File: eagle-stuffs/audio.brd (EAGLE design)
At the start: 57.1 x 44.5 mm, 23 parts, among them IC2 TL084P, IC3 DS1804-50k, IC4 DS1804-100k, U2 SSM2211SZ

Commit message: Added some info
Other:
- board text added: "Rev. A"
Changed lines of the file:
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@@
 <hole x="54.61" y="2.54" drill="2.8"/>
 <rectangle x1="34.29" y1="26.67" x2="39.37" y2="29.21" layer="41"/>
+<text x="44.45" y="38.1" size="1.778" layer="25">Rev. A</text>
 </plain>
 <attributes>

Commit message: Final version
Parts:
- removed IN: (no value), pinhead:1X02
- removed U2: SSM2211SZ, Analog Devices_By_element14_Batch_1:SOIC127P600X175-8N
- added D1: 1N5817, adafruit:DO41-7
- added IC1: SSM2211SZ, Analog Devices_By_element14_Batch_1:SOIC127P600X175-8N
- added LINE-IN: (no value), pinhead:1X02
- added R1: 2k, rcl:0204V
- added R11: 100k, rcl:0204V
- added R12: 15k, rcl:0204V
- added R13: 5.1k, rcl:0204V
- added R14: 20k, rcl:0204V
- added R2: 1k, rcl:0204V
- C1: value 250u -> 250; device rcl:E2-5 -> rcl:E3,5-10
- C2, C3: device rcl:C025-025X050 -> rcl:E3,5-8
- C4, C5: device rcl:C025-025X050 -> rcl:E2-4
- C6: value 2.2nF -> 10; device rcl:C025-025X050 -> rcl:E2-4
- IC4: value DS1804-100k -> DS1804-10k
- R10: device resistor:0207/10 -> rcl:0204V
- R3: value 20k -> 100k; device resistor:0207/10 -> rcl:0204V
- R4: value 15k -> 100k; device resistor:0207/10 -> rcl:0204V
- R5: value 10k -> 1M; device resistor:0207/10 -> rcl:0204V
- R6: value 33k -> 10k; device resistor:0207/10 -> rcl:0204V
- R7: value 1k -> 100; device resistor:0207/10 -> rcl:0204V
- R8: value 100k -> 10k; device resistor:0207/10 -> rcl:0204V
- R9: value 100k -> 1k; device resistor:0207/10 -> rcl:0204V
- moved R3 42.3 mm to (14.0, 5.08)
- moved R5 17.0 mm to (20.3, 7.62)
- moved R4 15.3 mm to (20.3, 5.08)
- moved C5 14.0 mm to (26.7, 6.35)
- moved R10 13.3 mm to (21.6, 22.9)
- moved R6 12.5 mm to (33.0, 5.08)
- moved C6 12.0 mm to (33.0, 10.2), turned to 180 degrees
- moved R8 11.5 mm to (33.0, 14.0)
- moved C4 10.9 mm to (6.35, 17.8)
- moved IC2 10.8 mm to (20.3, 15.2), turned to 0 degrees
- moved C1 10.2 mm to (48.3, 36.8)
- moved R9 6.35 mm to (26.7, 22.9)
- moved C2 5.24 mm to (41.9, 21.6), turned to 180 degrees
- moved C3 4.02 mm to (38.1, 36.8), turned to 180 degrees
- moved SPK 2.84 mm to (52.1, 29.2)
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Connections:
- removed net N$14: CTRL.9, IC2.7
- new net N$17: D1.A, IC2.7
- new net N$23: D1.C, IC2.5, R7.1
- new net N$24: C6.+, IC2.10, R7.2, R8.2
- new net N$25: IC2.9, R9.1
- new net N$26: IC2.8, R10.1, R9.2
- new net N$27: IC2.12, R10.2, R11.1
- new net N$28: CTRL.9, IC2.14, R11.2
- new net N$29: IC2.13, R12.2, R13.1
- new net N$7: IC4.6, R13.2
- net +5V: now also IC1.6, IC4.3, IC4.5, R1.2, R3.2; no longer R10.2, R5.2, R8.2, U2.6
- net GND: now also C3.-, C6.-, IC1.7, LINE-IN.1, R12.1, R8.1; no longer C3.2, C5.2, C6.2, IN.1, R9.1, U2.7
- net N$1: now also IC1.5; no longer U2.5
- net N$10: now also R2.2, R5.1; no longer IC4.5, R7.1
- net N$11: now also C5.+, R5.2; no longer IC4.6, R6.2
- net N$12: now also C5.-, R6.1; no longer IC2.6, R4.2, R5.1
- net N$13: now also IC2.6, R6.2; no longer C6.1, IC2.5, R6.1
- net N$15: now also R3.1, R4.2; no longer C5.1, R8.1, R9.2
- net N$2: now also C2.+, LINE-IN.2; no longer C2.1, IN.2
- net N$3: now also C2.-, R14.1; no longer C2.2, R3.2
- net N$4: now also IC1.4, IC3.6, R14.2; no longer R3.1, U2.4
- net N$5: now also C3.+, IC1.2, IC1.3; no longer C3.1, U2.2, U2.3
- net N$6: now also IC1.8; no longer U2.8
- net N$8: now also C4.-, R2.1; no longer C4.2, R7.2
- net N$9: now also C4.+, R1.1; no longer C4.1, R10.1
- net VCC: now also IC1.1; no longer U2.1
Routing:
- net N$14: track 46.8 -> 0.00 mm
- net GND: track 141.0 -> 101.0 mm
- net N$11: track 49.5 -> 15.1 mm
- net N$28: track 0.00 -> 33.4 mm
- net N$10: track 34.1 -> 7.62 mm
- net VCC: track 33.8 -> 58.1 mm
- net N$27: track 0.00 -> 22.5 mm
- net N$8: track 33.8 -> 12.4 mm
- net +5V: track 115.9 -> 136.1 mm
- net N$24: track 0.00 -> 20.2 mm
- net N$23: track 0.00 -> 20.0 mm
- net N$3: track 20.8 -> 4.42 mm
- net N$15: track 33.0 -> 17.6 mm
- net N$12: track 19.8 -> 4.64 mm
- net N$2: track 28.0 -> 13.0 mm
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- added copper zone on layer 16, net GND
- removed copper zone on layer 16, net N$16
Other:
- board text added: "+"

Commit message: C1 value changed
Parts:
- C1: value 250 -> 220
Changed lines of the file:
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@@
 <element name="R13" library="rcl" package="0204V" value="5.1k" x="16.51" y="22.86"/>
 <element name="R9" library="rcl" package="0204V" value="1k" x="26.67" y="22.86"/>
-<element name="C1" library="rcl" package="E3,5-10" value="250" x="48.26" y="36.83" smashed="yes">
+<element name="C1" library="rcl" package="E3,5-10" value="220" x="48.26" y="36.83" smashed="yes">
 <attribute name="NAME" x="45.974" y="33.909" size="1.27" layer="25" ratio="10"/>
 <attribute name="VALUE" x="44.958" y="33.782" size="1.27" layer="27" ratio="10"/>

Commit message: adjusted value of digital pot
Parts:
- IC3: value DS1804-50k -> DS1804-100k
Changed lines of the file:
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@@
 <attribute name="VALUE" x="13.589" y="14.605" size="1.27" layer="27" ratio="10"/>
 </element>
-<element name="IC3" library="pot-xicor" package="DIL08" value="DS1804-50k" x="24.13" y="30.48" smashed="yes">
+<element name="IC3" library="pot-xicor" package="DIL08" value="DS1804-100k" x="24.13" y="30.48" smashed="yes">
 <attribute name="OC_NEWARK" value="51J6928" x="24.13" y="30.48" size="1.778" layer="27" display="off"/>
 <attribute name="MPN" value="X9C102P" x="24.13" y="30.48" size="1.778" layer="27" display="off"/>

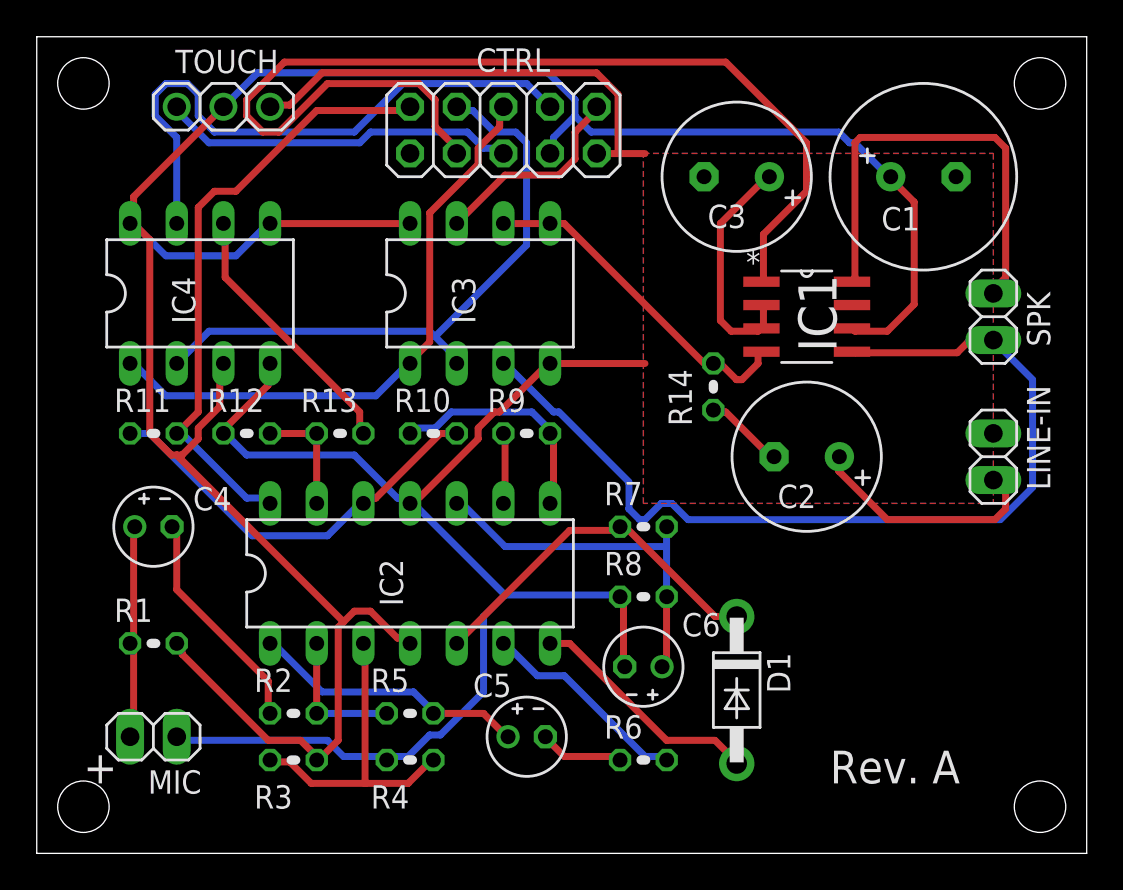
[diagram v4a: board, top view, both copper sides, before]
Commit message: Added voltage divider on output
I forgot I was dealing with 3.3v input chip! :-(
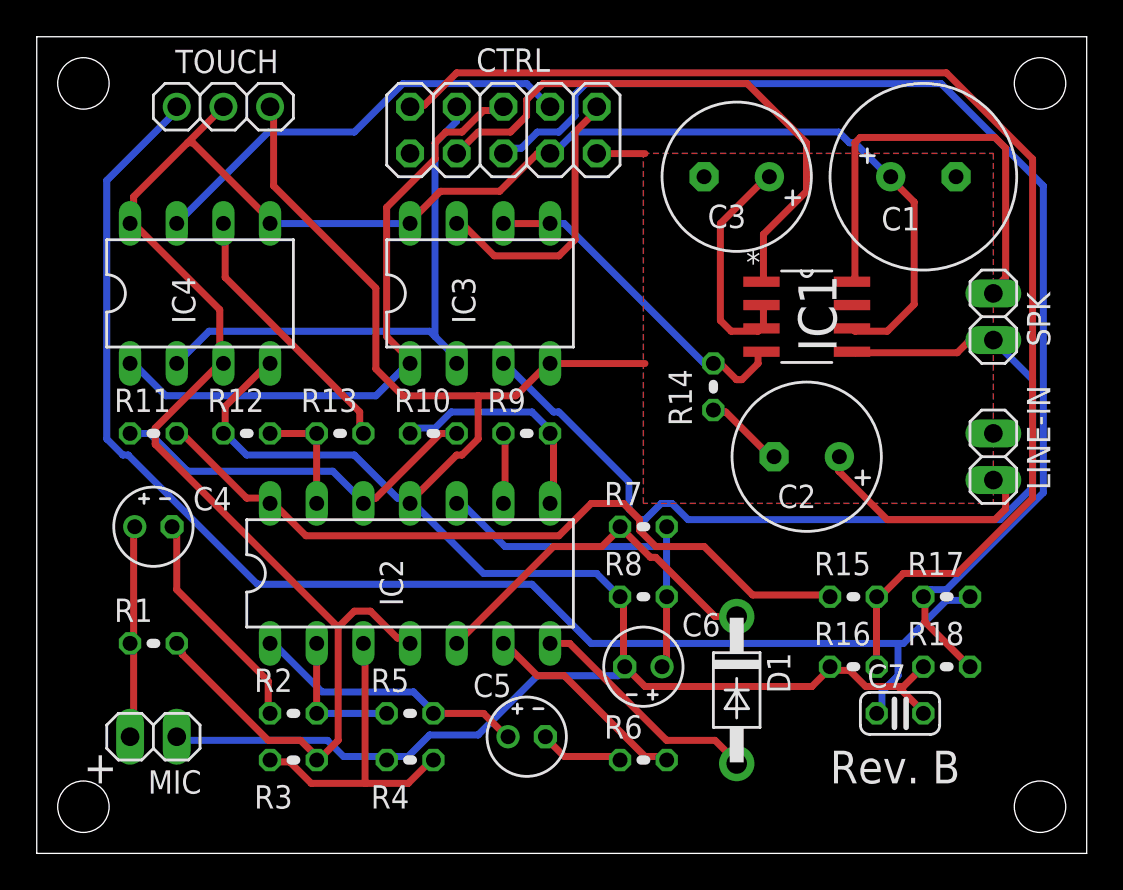
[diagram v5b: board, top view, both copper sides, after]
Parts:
- added C7: 0.1, rcl:C025-024X044
- added R15, R16, R17, R18: 10k, rcl:0204V
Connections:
- removed net N$22: CTRL.6, TOUCH.1
- new net N$14: IC2.14, R11.2, R15.1
- new net N$16: CTRL.9, R15.2, R16.2
- new net N$30: CTRL.6, R17.1, R18.2
- net GND: now also C7.2, R16.1, R18.1
- net N$28: now also C7.1, R17.2, TOUCH.1; no longer CTRL.9, IC2.14, R11.2
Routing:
- net N$16: track 0.00 -> 69.5 mm
- net N$30: track 0.00 -> 64.5 mm
- net N$28: track 33.4 -> 76.6 mm
- net N$14: track 0.00 -> 41.1 mm
- net VCC: track 58.1 -> 31.0 mm
- net GND: track 101.0 -> 124.2 mm
- net N$22: track 19.5 -> 0.00 mm
- net +5V: track 136.1 -> 117.0 mm
- net N$19: track 32.6 -> 24.0 mm
- net N$21: track 34.1 -> 29.8 mm
- net N$18: track 11.2 -> 15.3 mm
- net N$20: track 32.7 -> 34.8 mm
- net N$27: track 22.5 -> 21.1 mm
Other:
- board text added: "Rev. B"
- board text removed: "Rev. A"

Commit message: Removed second digital pot
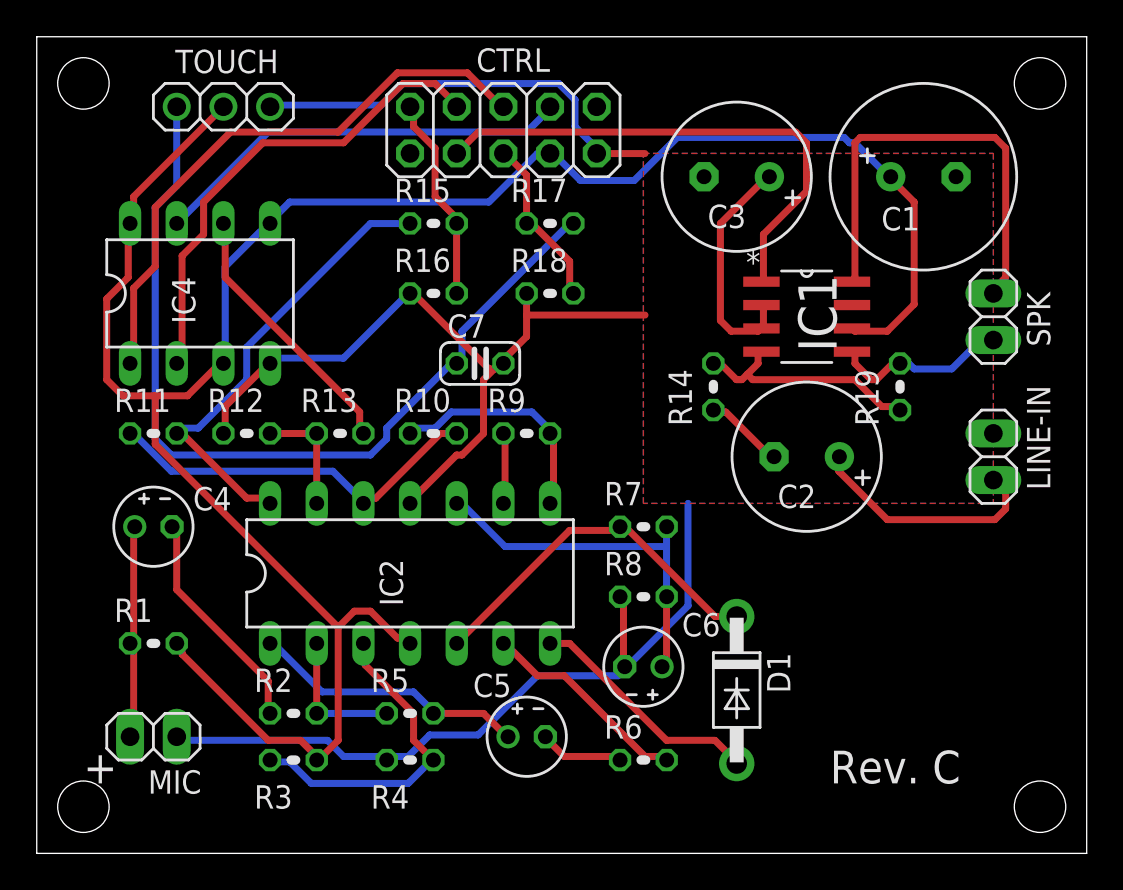
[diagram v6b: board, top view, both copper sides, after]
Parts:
- removed IC3: DS1804-100k, pot-xicor:DIL08
- added R19: 33k, rcl:0204V
- R14: value 20k -> 22k
- moved R15 30.6 mm to (21.6, 34.3)
- moved R16 30.6 mm to (21.6, 30.5)
- moved C7 29.8 mm to (24.1, 26.7)
- moved R17 29.6 mm to (27.9, 34.3)
- moved R18 29.6 mm to (27.9, 30.5)
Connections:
- removed net N$18: CTRL.1, IC3.7
- net +5V: no longer IC3.8
- net GND: no longer IC3.4
- net N$1: now also R19.2; no longer IC3.3
- net N$20: no longer IC3.1
- net N$21: no longer IC3.2
- net N$4: now also R19.1; no longer IC3.5, IC3.6
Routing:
- net N$16: track 69.5 -> 11.2 mm
- net N$30: track 64.5 -> 9.38 mm
- net N$1: track 51.5 -> 10.4 mm
- net N$28: track 76.6 -> 48.5 mm
- net GND: track 124.2 -> 106.7 mm
- net N$14: track 41.1 -> 25.2 mm
- net N$18: track 15.3 -> 0.00 mm
- net +5V: track 117.0 -> 123.6 mm
- net N$4: track 19.3 -> 13.4 mm
- net N$21: track 29.8 -> 26.4 mm
- net N$20: track 34.8 -> 31.8 mm
- net VCC: track 31.0 -> 28.3 mm
- net N$19: track 24.0 -> 23.0 mm
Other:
- board text added: "Rev. C"
- board text removed: "Rev. B"

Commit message: Inverted input on follower section for mic
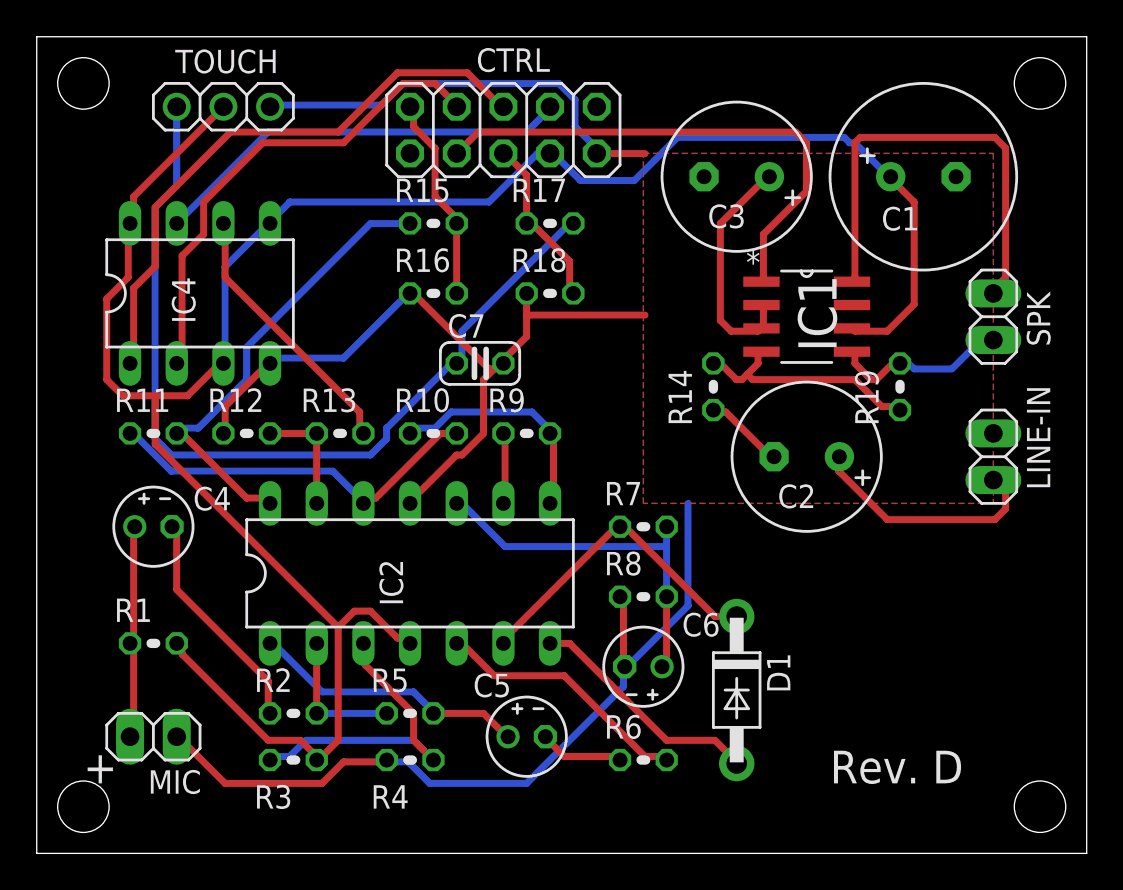
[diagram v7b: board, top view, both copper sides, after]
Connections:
- removed net N$13: IC2.6, R6.2
- new net N$18: IC2.5, R6.2
- net N$23: now also IC2.6; no longer IC2.5
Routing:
- net N$18: track 0.00 -> 14.2 mm
- net N$13: track 11.6 -> 0.00 mm
- net GND: track 106.7 -> 109.2 mm
- net N$23: track 20.0 -> 17.6 mm
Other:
- board text added: "Rev. D"
- board text removed: "Rev. C"
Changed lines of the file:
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@@
 <hole x="54.61" y="41.91" drill="2.8"/>
 <hole x="54.61" y="2.54" drill="2.8"/>
-<text x="43.18" y="3.81" size="1.778" layer="25">Rev. C</text>
+<text x="43.18" y="3.81" size="1.778" layer="25">Rev. D</text>
 <rectangle x1="40.64" y1="26.67" x2="43.18" y2="31.75" layer="41"/>
 <text x="2.54" y="3.81" size="1.778" layer="25">+</text>
@@
 <wire x1="12.892" y1="26.956" x2="12.7" y2="26.67" width="0.381" layer="16"/>
 <wire x1="20.217" y1="30.472" x2="20.32" y2="30.48" width="0.381" layer="16"/>
-<wire x1="16.701" y1="5.274" x2="19.045" y2="5.274" width="0.381" layer="16"/>
-<wire x1="15.822" y1="6.153" x2="16.701" y2="5.274" width="0.381" layer="16"/>
-<wire x1="7.911" y1="6.153" x2="15.822" y2="6.153" width="0.381" layer="16"/>
-<wire x1="19.045" y1="5.274" x2="19.05" y2="5.08" width="0.381" layer="16"/>
-<wire x1="7.911" y1="6.153" x2="7.62" y2="6.35" width="0.381" layer="16"/>
+<wire x1="16.701" y1="4.981" x2="19.045" y2="4.981" width="0.381" layer="1"/>
+<wire x1="15.529" y1="3.809" x2="16.701" y2="4.981" width="0.381" layer="1"/>
+<wire x1="10.255" y1="3.809" x2="15.529" y2="3.809" width="0.381" layer="1"/>
+<wire x1="7.911" y1="6.153" x2="10.255" y2="3.809" width="0.381" layer="1"/>
+<wire x1="19.045" y1="4.981" x2="19.05" y2="5.08" width="0.381" layer="1"/>
+<wire x1="7.911" y1="6.153" x2="7.62" y2="6.35" width="0.381" layer="1"/>
 <wire x1="31.937" y1="10.255" x2="31.937" y2="13.771" width="0.381" layer="1"/>
 <wire x1="31.937" y1="13.771" x2="31.75" y2="13.97" width="0.381" layer="1"/>
@@
 <wire x1="35.453" y1="19.05" x2="35.453" y2="13.478" width="0.381" layer="16"/>
 <wire x1="32.23" y1="10.255" x2="32.004" y2="10.16" width="0.381" layer="16"/>
-<wire x1="20.217" y1="5.274" x2="19.338" y2="5.274" width="0.381" layer="16"/>
-<wire x1="21.389" y1="6.446" x2="20.217" y2="5.274" width="0.381" layer="16"/>
-<wire x1="24.026" y1="6.446" x2="21.389" y2="6.446" width="0.381" layer="16"/>
-<wire x1="27.249" y1="9.669" x2="24.026" y2="6.446" width="0.381" layer="16"/>
-<wire x1="31.644" y1="9.669" x2="27.249" y2="9.669" width="0.381" layer="16"/>
-<wire x1="31.937" y1="9.962" x2="31.644" y2="9.669" width="0.381" layer="16"/>
-<wire x1="19.338" y1="5.274" x2="19.05" y2="5.08" width="0.381" layer="16"/>
+<wire x1="20.217" y1="4.981" x2="19.338" y2="4.981" width="0.381" layer="16"/>
+<wire x1="21.389" y1="3.809" x2="20.217" y2="4.981" width="0.381" layer="16"/>
+<wire x1="26.663" y1="3.809" x2="21.389" y2="3.809" width="0.381" layer="16"/>
+<wire x1="31.937" y1="9.083" x2="26.663" y2="3.809" width="0.381" layer="16"/>
+<wire x1="31.937" y1="9.962" x2="31.937" y2="9.083" width="0.381" layer="16"/>
+<wire x1="19.338" y1="4.981" x2="19.05" y2="5.08" width="0.381" layer="16"/>
 <wire x1="31.937" y1="9.962" x2="32.004" y2="10.16" width="0.381" layer="16"/>
 <wire x1="33.109" y1="29.3" x2="26.663" y2="29.3" width="0.381" layer="1"/>
@@
 <contactref element="R3" pad="1"/>
 <contactref element="R4" pad="2"/>
-<wire x1="13.771" y1="4.981" x2="12.892" y2="4.981" width="0.381" layer="16"/>
-<wire x1="14.943" y1="3.809" x2="13.771" y2="4.981" width="0.381" layer="16"/>
-<wire x1="20.217" y1="3.809" x2="14.943" y2="3.809" width="0.381" layer="16"/>
-<wire x1="21.389" y1="4.981" x2="20.217" y2="3.809" width="0.381" layer="16"/>
-<wire x1="12.892" y1="4.981" x2="12.7" y2="5.08" width="0.381" layer="16"/>
-<wire x1="21.389" y1="4.981" x2="21.59" y2="5.08" width="0.381" layer="16"/>
+<wire x1="13.771" y1="5.274" x2="12.892" y2="5.274" width="0.381" layer="16"/>
+<wire x1="14.65" y1="6.153" x2="13.771" y2="5.274" width="0.381" layer="16"/>
+<wire x1="20.51" y1="6.153" x2="14.65" y2="6.153" width="0.381" layer="16"/>
+<wire x1="21.389" y1="5.274" x2="20.51" y2="6.153" width="0.381" layer="16"/>
+<wire x1="12.892" y1="5.274" x2="12.7" y2="5.08" width="0.381" layer="16"/>
+<wire x1="21.389" y1="5.274" x2="21.59" y2="5.08" width="0.381" layer="16"/>
 <wire x1="17.873" y1="10.255" x2="17.873" y2="11.427" width="0.381" layer="1"/>
 <wire x1="20.51" y1="7.618" x2="17.873" y2="10.255" width="0.381" layer="1"/>
@@
 <wire x1="27.835" y1="6.153" x2="27.686" y2="6.35" width="0.381" layer="1"/>
 </signal>
-<signal name="N$13">
-<contactref element="IC2" pad="6"/>
-<contactref element="R6" pad="2"/>
-<wire x1="33.109" y1="5.274" x2="34.281" y2="5.274" width="0.381" layer="1"/>
-<wire x1="28.714" y1="9.669" x2="33.109" y2="5.274" width="0.381" layer="1"/>
-<wire x1="27.249" y1="9.669" x2="28.714" y2="9.669" width="0.381" layer="1"/>
-<wire x1="25.491" y1="11.427" x2="27.249" y2="9.669" width="0.381" layer="1"/>
-<wire x1="34.281" y1="5.274" x2="34.29" y2="5.08" width="0.381" layer="1"/>
-<wire x1="25.491" y1="11.427" x2="25.4" y2="11.43" width="0.381" layer="1"/>
-</signal>
 <signal name="N$17">
 <contactref element="IC2" pad="7"/>
@@
 </signal>
 <signal name="N$23">
-<contactref element="IC2" pad="5"/>
 <contactref element="D1" pad="C"/>
 <contactref element="R7" pad="1"/>
-<wire x1="29.007" y1="17.58" x2="23.147" y2="11.72" width="0.381" layer="1"/>
-<wire x1="31.644" y1="17.58" x2="29.007" y2="17.58" width="0.381" layer="1"/>
-<wire x1="23.147" y1="11.72" x2="22.86" y2="11.43" width="0.381" layer="1"/>
-<wire x1="31.644" y1="17.58" x2="31.75" y2="17.78" width="0.381" layer="1"/>
+<contactref element="IC2" pad="6"/>
+<wire x1="31.644" y1="17.873" x2="25.491" y2="11.72" width="0.381" layer="1"/>
+<wire x1="25.491" y1="11.72" x2="25.4" y2="11.43" width="0.381" layer="1"/>
+<wire x1="31.644" y1="17.873" x2="31.75" y2="17.78" width="0.381" layer="1"/>
 <wire x1="36.918" y1="12.892" x2="38.09" y2="12.892" width="0.381" layer="1"/>
 <wire x1="31.937" y1="17.873" x2="36.918" y2="12.892" width="0.381" layer="1"/>
@@
 <wire x1="26.956" y1="34.281" x2="26.67" y2="34.29" width="0.381" layer="1"/>
 </signal>
+<signal name="N$18">
+<contactref element="R6" pad="2"/>
+<contactref element="IC2" pad="5"/>
+<wire x1="33.109" y1="5.274" x2="34.281" y2="5.274" width="0.381" layer="1"/>
+<wire x1="28.714" y1="9.669" x2="33.109" y2="5.274" width="0.381" layer="1"/>
+<wire x1="24.905" y1="9.669" x2="28.714" y2="9.669" width="0.381" layer="1"/>
+<wire x1="23.147" y1="11.427" x2="24.905" y2="9.669" width="0.381" layer="1"/>
+<wire x1="34.281" y1="5.274" x2="34.29" y2="5.08" width="0.381" layer="1"/>
+<wire x1="23.147" y1="11.427" x2="22.86" y2="11.43" width="0.381" layer="1"/>
+</signal>
 </signals>
